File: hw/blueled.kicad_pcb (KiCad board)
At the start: 2 copper layers, 33 x 61 mm, 31 parts, among them J1 Barrel_Jack, J2 LED Strip, J3 ICSP, Q1 Q_PMOS_SDG, Q2 Q_PNP_EBC, SW2 PUSH, U1 ATmega328P-AU, U2 HC-05, U3 AMS1117-3.3, U4 AT25SF081

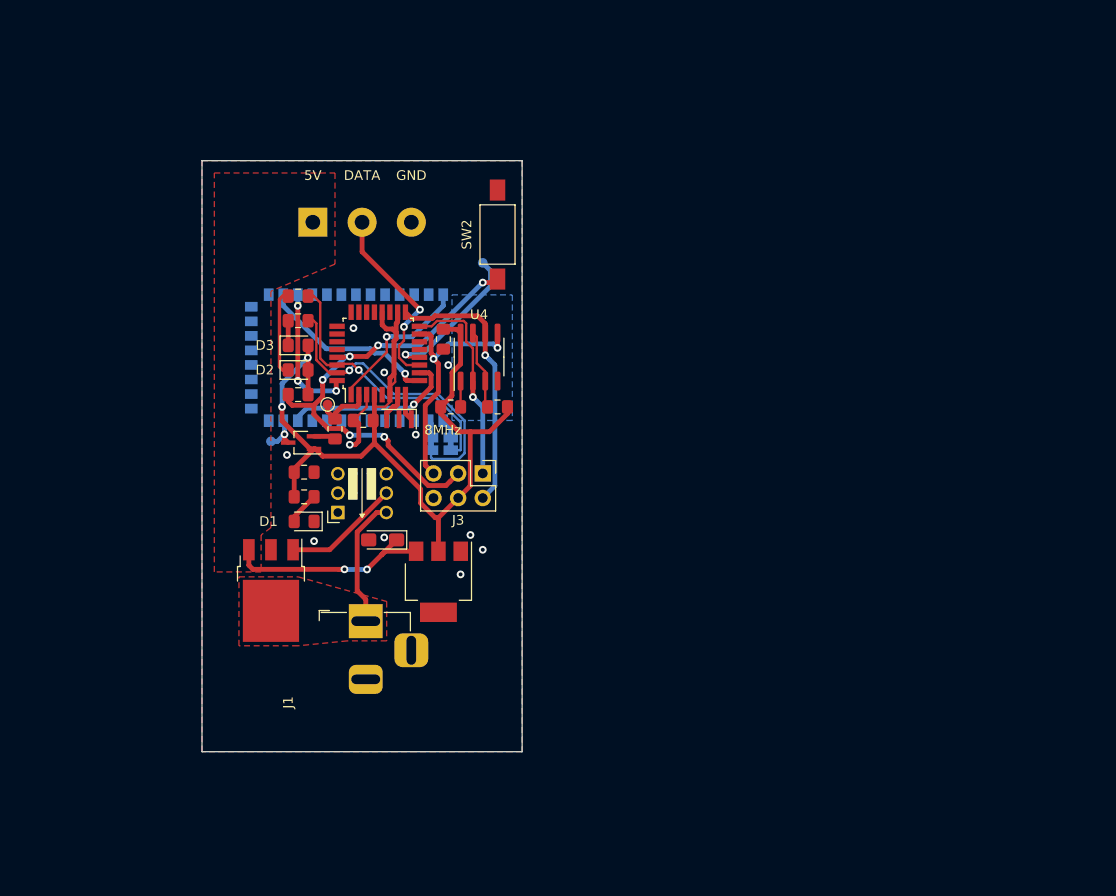
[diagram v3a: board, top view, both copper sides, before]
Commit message: add(hw): board sizes according to ISO/IEC 7810 ID-1
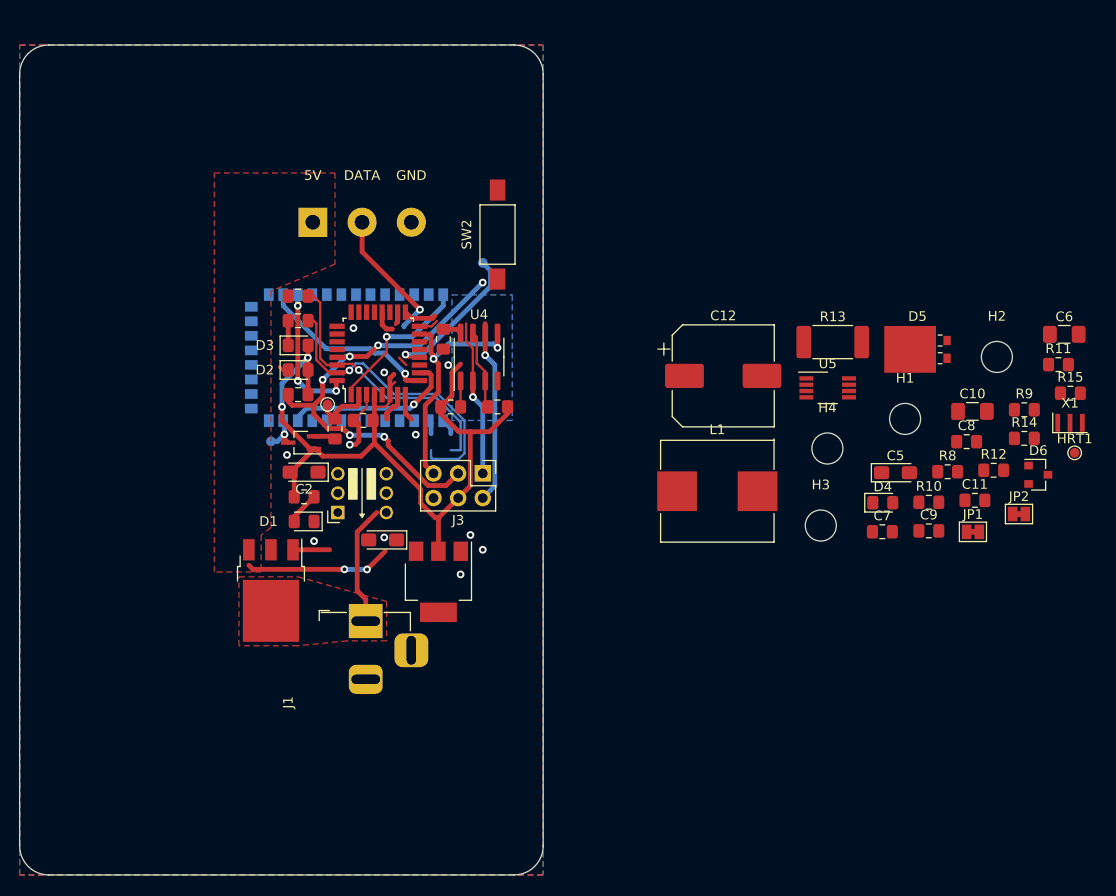
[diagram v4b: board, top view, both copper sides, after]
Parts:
- removed 8MHz: RESON-MURATA-CSTCE, blueled:Resonator_SMD_muRata_CSTNE_3Pin_3.2x1.3mm
- removed RX, TX: Jumper_NC_Small, Jumper:SolderJumper-2_P1.3mm_Bridged_Pad1.0x1.5mm
- added C10: 100uF, Capacitor_SMD:C_1206_3216Metric_Pad1.42x1.75mm_HandSolder, F.Cu at (218.3, 100.8)
- added C11: 1nF, Capacitor_SMD:C_0805_2012Metric_Pad1.15x1.40mm_HandSolder, F.Cu at (218.5, 110.0)
- added C12: 1000uF, Capacitor_SMD:CP_Elec_10x10, F.Cu at (192.6, 97.1)
- added C5: 22uF, Capacitor_Tantalum_SMD:CP_EIA-3216-18_Kemet-A_Pad1.58x1.35mm_HandSolder, F.Cu at (210.3, 107.1)
- added C6: 4.7uF, Capacitor_SMD:C_1206_3216Metric_Pad1.42x1.75mm_HandSolder, F.Cu at (227.7, 92.8)
- added C7: 680nF, Capacitor_SMD:C_0805_2012Metric_Pad1.15x1.40mm_HandSolder, F.Cu at (209.0, 113.2)
- added C8: 0.47uF, Capacitor_SMD:C_0805_2012Metric_Pad1.15x1.40mm_HandSolder, F.Cu at (217.7, 103.9)
- added C9: 0.1uF, Capacitor_SMD:C_0805_2012Metric_Pad1.15x1.40mm_HandSolder, F.Cu at (213.8, 113.1)
- added D4: +5V, LED_SMD:LED_0805_2012Metric_Pad1.15x1.40mm_HandSolder, F.Cu at (209.0, 110.2)
- added D5: MBRB2060, Diode_SMD:D_Powermite3, F.Cu at (212.6, 94.4)
- added D6: BAS40-04, Package_TO_SOT_SMD:SOT-23, F.Cu at (225.1, 107.3)
- added H1: MountingHole_Pad, MountingHole:MountingHole_3.2mm_M3, F.Cu at (211.3, 101.6)
- added H2: MountingHole_Pad, MountingHole:MountingHole_3.2mm_M3, F.Cu at (220.8, 95.2)
- added H3: MountingHole_Pad, MountingHole:MountingHole_3.2mm_M3, F.Cu at (202.6, 112.6)
- added H4: MountingHole_Pad, MountingHole:MountingHole_3.2mm_M3, F.Cu at (203.3, 104.6)
- added HRT1: Heartbeat, TestPoint:TestPoint_Pad_D1.0mm, F.Cu at (228.8, 105.1)
- added JP1: Jumper_NC_Small, Jumper:SolderJumper-2_P1.3mm_Bridged_Pad1.0x1.5mm, F.Cu at (218.3, 113.2)
- added JP2: Jumper_NC_Small, Jumper:SolderJumper-2_P1.3mm_Bridged_Pad1.0x1.5mm, F.Cu at (223.1, 111.4)
- added L1: 15uH, blueled:SMMS1350-150M, F.Cu at (192.0, 109.0)
- added R10: 10k, Resistor_SMD:R_0805_2012Metric_Pad1.15x1.40mm_HandSolder, F.Cu at (213.8, 110.2)
- added R11: 470, Resistor_SMD:R_0805_2012Metric_Pad1.15x1.40mm_HandSolder, F.Cu at (227.1, 96.0)
- added R12: 2.1k, Resistor_SMD:R_0805_2012Metric_Pad1.15x1.40mm_HandSolder, F.Cu at (220.5, 106.9)
- added R13: 0.01, Resistor_SMD:R_2512_6332Metric_Pad1.52x3.35mm_HandSolder, F.Cu at (203.9, 93.6)
- added R14: 10k, Resistor_SMD:R_0805_2012Metric_Pad1.15x1.40mm_HandSolder, F.Cu at (223.6, 103.6)
- added R15: 470, Resistor_SMD:R_0805_2012Metric_Pad1.15x1.40mm_HandSolder, F.Cu at (228.4, 98.9)
- added R8: 90.9, Resistor_SMD:R_0805_2012Metric_Pad1.15x1.40mm_HandSolder, F.Cu at (215.7, 107.0)
- added R9: 3.4k, Resistor_SMD:R_0805_2012Metric_Pad1.15x1.40mm_HandSolder, F.Cu at (223.6, 100.6)
- added U5: LM25085MM, Package_SO:VSSOP-8_3.0x3.0mm_P0.65mm, F.Cu at (203.3, 98.4)
- added X1: CSTCE, blueled:Resonator_SMD_muRata_CSTNE_3Pin_3.2x1.3mm, F.Cu at (228.3, 102.0)
- C2: value 10uF -> 22uF; footprint Capacitor_SMD:C_0805_2012Metric_Pad1.15x1.40mm_HandSolder -> Capacitor_Tantalum_SMD:CP_EIA-3216-18_Kemet-A_Pad1.58x1.35mm_HandSolder
- D1: value LED -> +3.3V
- R2, R3, R6: value 1k -> 150
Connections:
- C1 pad 1: /VIN -> +5V
- Q1 pad 1: /VIN -> Net-(D5-Pad1)
- Q1 pad 2: /VINJACK -> Net-(Q1-Pad2)
- S1 pad 1: Net-(S1-Pad1) -> (no net)
- S1 pad 2: Net-(S1-Pad2) -> (no net)
- S1 pad 3: Net-(S1-Pad3) -> (no net)
- S1 pad 4: GND -> (no net)
- S1 pad 5: Net-(Q1-Pad3) -> /SHUTDOWN
- S1 pad 6: /VINJACK -> GND
- U1 pad 11: /DATA -> Net-(R11-Pad1)
- U1 pad 14: Net-(U1-Pad14) -> (no net)
- U1 pad 19: Net-(U1-Pad19) -> (no net)
- U1 pad 22: Net-(U1-Pad22) -> (no net)
- U1 pad 23: Net-(U1-Pad23) -> (no net)
- U1 pad 24: Net-(U1-Pad24) -> (no net)
- U1 pad 25: Net-(U1-Pad25) -> (no net)
- U1 pad 26: Net-(U1-Pad26) -> (no net)
- U1 pad 27: Net-(U1-Pad27) -> (no net)
- U1 pad 28: Net-(U1-Pad28) -> (no net)
- U2 pad 10: Net-(U2-Pad10) -> (no net)
- U2 pad 15: Net-(U2-Pad15) -> (no net)
- U2 pad 16: Net-(U2-Pad16) -> (no net)
- U2 pad 17: Net-(U2-Pad17) -> (no net)
- U2 pad 18: Net-(U2-Pad18) -> (no net)
- U2 pad 19: Net-(U2-Pad19) -> (no net)
- U2 pad 20: Net-(U2-Pad20) -> (no net)
- U2 pad 25: Net-(U2-Pad25) -> (no net)
- U2 pad 26: Net-(U2-Pad26) -> (no net)
- U2 pad 27: Net-(U2-Pad27) -> (no net)
- U2 pad 28: Net-(U2-Pad28) -> (no net)
- U2 pad 29: Net-(U2-Pad29) -> (no net)
- U2 pad 3: Net-(U2-Pad3) -> (no net)
- U2 pad 30: Net-(U2-Pad30) -> (no net)
- U2 pad 31: Net-(U2-Pad31) -> (no net)
- U2 pad 32: Net-(U2-Pad32) -> (no net)
- U2 pad 33: Net-(U2-Pad33) -> (no net)
- U2 pad 4: Net-(U2-Pad4) -> (no net)
- U2 pad 5: Net-(U2-Pad5) -> (no net)
- U2 pad 6: Net-(U2-Pad6) -> (no net)
- U2 pad 7: Net-(U2-Pad7) -> (no net)
- U2 pad 8: Net-(U2-Pad8) -> (no net)
- U2 pad 9: Net-(U2-Pad9) -> (no net)
- U3 pad 3: /VIN -> +5V
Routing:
- net +3V3: track 104.9 -> 89.1 mm
- net Net-(Q1-Pad3): track 12.0 -> 3.78 mm
- net Net-(D2-Pad1): track 9.04 -> 1.03 mm
- net /VIN: track 22.0 -> 15.0 mm
- net /SCK: track 27.8 -> 22.3 mm
- net /DATA: track 19.8 -> 15.0 mm, vias 2 -> 1
- net /MISO: track 21.3 -> 18.2 mm
- net /RESET: track 49.9 -> 48.2 mm
- net /MOSI: track 25.6 -> 24.6 mm
- net /VINJACK: track 13.4 -> 12.4 mm
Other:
- board size 33 x 61 mm -> 54 x 85.6 mm

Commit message: refactor(hw): removing old traces and rearrangments
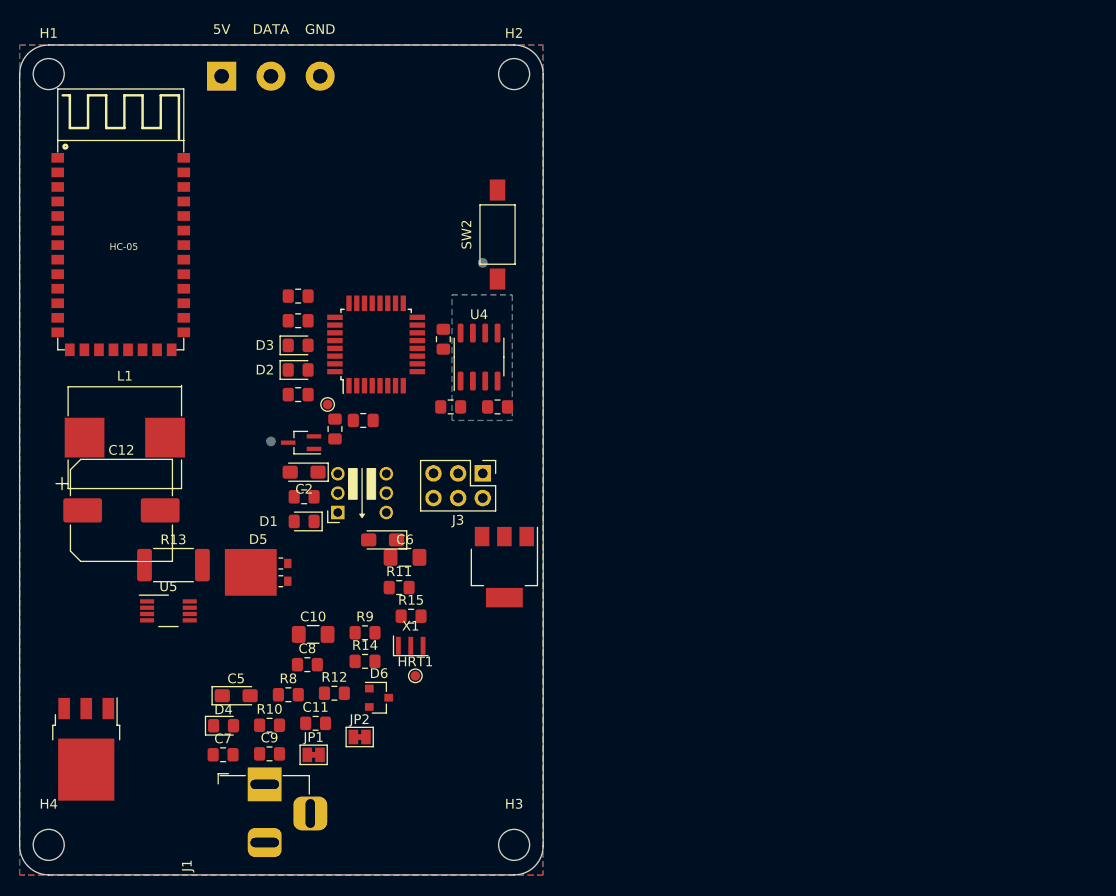
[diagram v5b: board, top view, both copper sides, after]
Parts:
- U2: moved to F.Cu
- moved H1 95.2 mm to (123.0, 66.0)
- moved H4 90.1 mm to (123.0, 145.5)
- moved C10 71.8 mm to (150.3, 123.8)
- moved C11 71.8 mm to (150.5, 133.0)
- moved C5 71.8 mm to (142.3, 130.1)
- moved C6 71.8 mm to (159.7, 115.8)
- moved C7 71.8 mm to (141.0, 136.2)
- moved C8 71.8 mm to (149.7, 126.9)
- moved C9 71.8 mm to (145.8, 136.1)
- moved D4 71.8 mm to (141.0, 133.2)
- moved D5 71.8 mm to (144.6, 117.4)
- moved HRT1 71.8 mm to (160.8, 128.1)
- moved JP1 71.8 mm to (150.3, 136.2)
- moved JP2 71.8 mm to (155.1, 134.4)
- moved R11 71.8 mm to (159.1, 119.0)
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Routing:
- net +3V3: track 89.1 -> 0.00 mm, vias 2 -> 0
- net /RESET: track 48.2 -> 0.00 mm, vias 6 -> 0
- net /TX: track 31.5 -> 0.00 mm, vias 1 -> 0
- net /RX: track 28.5 -> 0.00 mm, vias 1 -> 0
- net /MOSI: track 24.6 -> 0.00 mm, vias 2 -> 0
- net /SCK: track 22.3 -> 0.00 mm, vias 1 -> 0
- net /HC-DISCNCT: track 18.7 -> 0.00 mm, vias 1 -> 0
- net /MISO: track 18.2 -> 0.00 mm, vias 1 -> 0
- net /HC-RESET: track 18.0 -> 0.00 mm, vias 1 -> 0
- net Net-(DBG0-Pad1): track 16.0 -> 0.00 mm, vias 1 -> 0
- net /HC-ATMODE: track 15.8 -> 0.00 mm, vias 1 -> 0
- net /DATA: track 15.0 -> 0.00 mm, vias 1 -> 0
- net /VIN: track 15.0 -> 0.00 mm, vias 2 -> 0
- net /HC-STATE: track 14.4 -> 0.00 mm, vias 3 -> 0
- net /VINJACK: track 12.4 -> 0.00 mm
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- removed copper zone on F.Cu, net /VIN
- removed copper zone on F.Cu, net /VINJACK

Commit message: add(hw): initial layout for v2.0
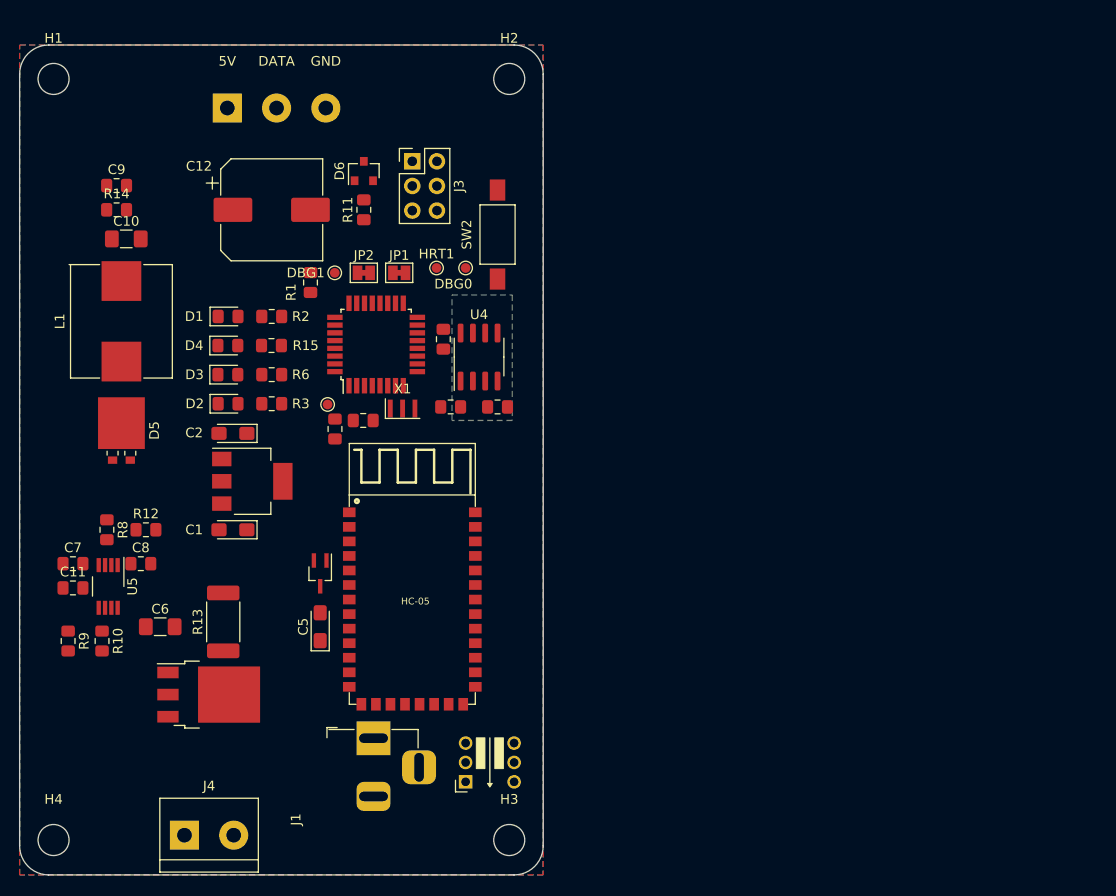
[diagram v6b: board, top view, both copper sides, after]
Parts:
- added J4: Screw_Terminal_01x02, TerminalBlock:TerminalBlock_bornier-2_P5.08mm, F.Cu at (137.0, 144.5)
- DBG0, DBG1: moved to F.Cu
- moved C9 60.7 mm to (130.0, 77.5)
- moved D6 54.3 mm to (155.5, 76.0), turned to 90 degrees
- moved R14 53.2 mm to (130.0, 80.0)
- moved JP1 50.5 mm to (159.2, 86.5)
- moved JP2 47.9 mm to (155.5, 86.5)
- moved U2 47.3 mm to (160.5, 131.0)
- moved C10 45.1 mm to (131.0, 83.0)
- moved HRT1 42.1 mm to (163.0, 86.0)
- moved D4 39.2 mm to (141.5, 94.0)
- moved R11 39.1 mm to (155.5, 80.0), turned to 90 degrees
- moved C12 34.7 mm to (146.0, 80.0)
- moved J3 33.0 mm to (160.5, 75.0), turned to 0 degrees
- moved R15 31.4 mm to (146.0, 94.0)
- moved S1 30.7 mm to (168.5, 137.0)
- moved R9 30.6 mm to (125.0, 124.5), turned to 270 degrees
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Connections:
- C12 pad 1: /VIN -> (no net)
- J2 pad 1: /VIN -> +5V
- R4 pad 2: Net-(R4-Pad2) -> /~CS-FLASH
- U1 pad 14: (no net) -> /~CS-FLASH
- U4 pad 1: Net-(R4-Pad2) -> /~CS-FLASH

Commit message: add(hw): more layout improvements
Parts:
- moved DBG1 32.6 mm to (150.5, 119.0)
- moved R1 14.6 mm to (152.0, 102.0), turned to 90 degrees
- moved DBG2 13.6 mm to (152.5, 86.5)
- moved R5 9.94 mm to (153.5, 112.5)
- moved C4 4.70 mm to (165.5, 89.0), turned to 90 degrees
- moved C5 2.50 mm to (153.5, 123.0), turned to 270 degrees
- moved Q2 2.50 mm to (153.5, 117.5)
- moved U2 2.50 mm to (163.0, 131.0)
- moved R4 1.64 mm to (165.6, 101.5), turned to 90 degrees
- moved X1 1.41 mm to (158.5, 101.5)
- moved R7 1.19 mm to (169.5, 101.5), turned to 270 degrees
- moved C1 1.00 mm to (142.0, 114.0)
- moved C3 0.52 mm to (155.0, 102.0), turned to 90 degrees
- moved U3 0.50 mm to (144.0, 108.5)
